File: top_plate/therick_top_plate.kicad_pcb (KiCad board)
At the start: 2 copper layers, 227.8 x 75.5 mm, 54 parts, among them U1 HOLE, U10 HOLE, U11 HOLE, U12 HOLE, U13 HOLE, U14 HOLE, U15 HOLE, U16 HOLE, U17 HOLE, U18 HOLE, U19 HOLE, U2 HOLE, U20 HOLE, U21 HOLE, U22 HOLE, U23 HOLE, U24 HOLE, U25 HOLE, U26 HOLE, U27 HOLE, U28 HOLE, U29 HOLE, U3 HOLE, U30 HOLE, U31 HOLE, U32 HOLE, U33 HOLE, U34 HOLE, U35 HOLE, U36 HOLE, U37 HOLE, U38 HOLE, U39 HOLE, U4 HOLE, U40 HOLE, U41 HOLE, U42 HOLE, U43 HOLE, U44 HOLE, U45 HOLE, U46 HOLE, U47 HOLE, U48 HOLE, U5 HOLE, U6 HOLE, U7 HOLE, U8 HOLE, U9 HOLE

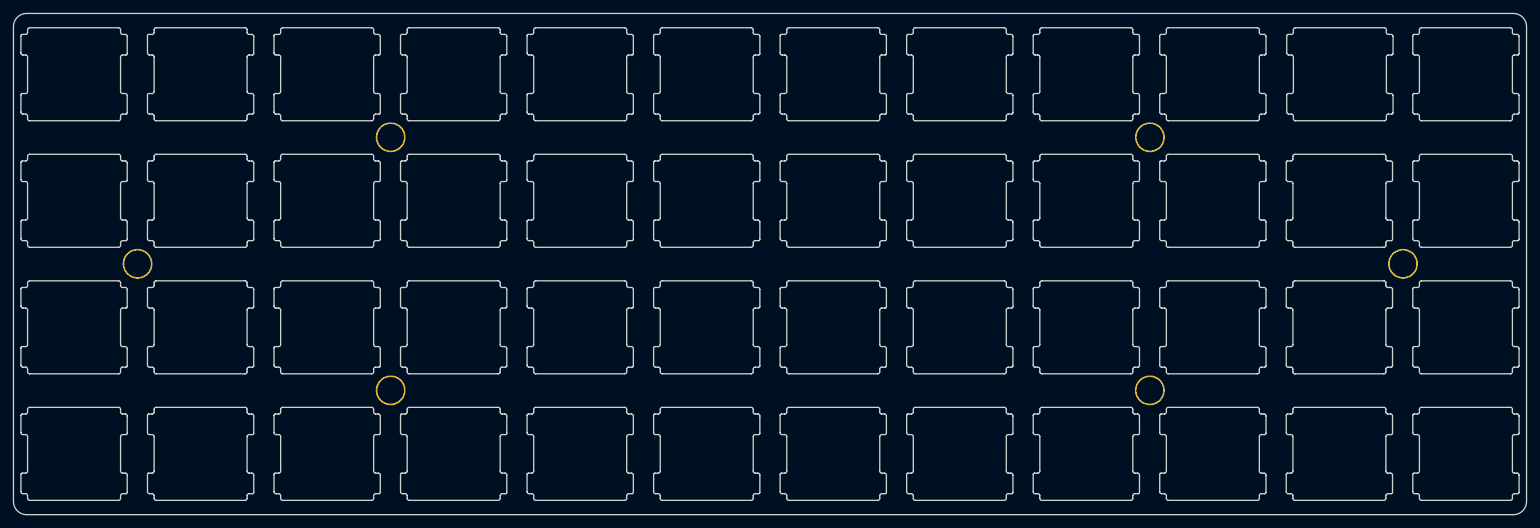
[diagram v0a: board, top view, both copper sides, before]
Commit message: Removed Type C Connector
Only uses a Pro Micro/Elite C now
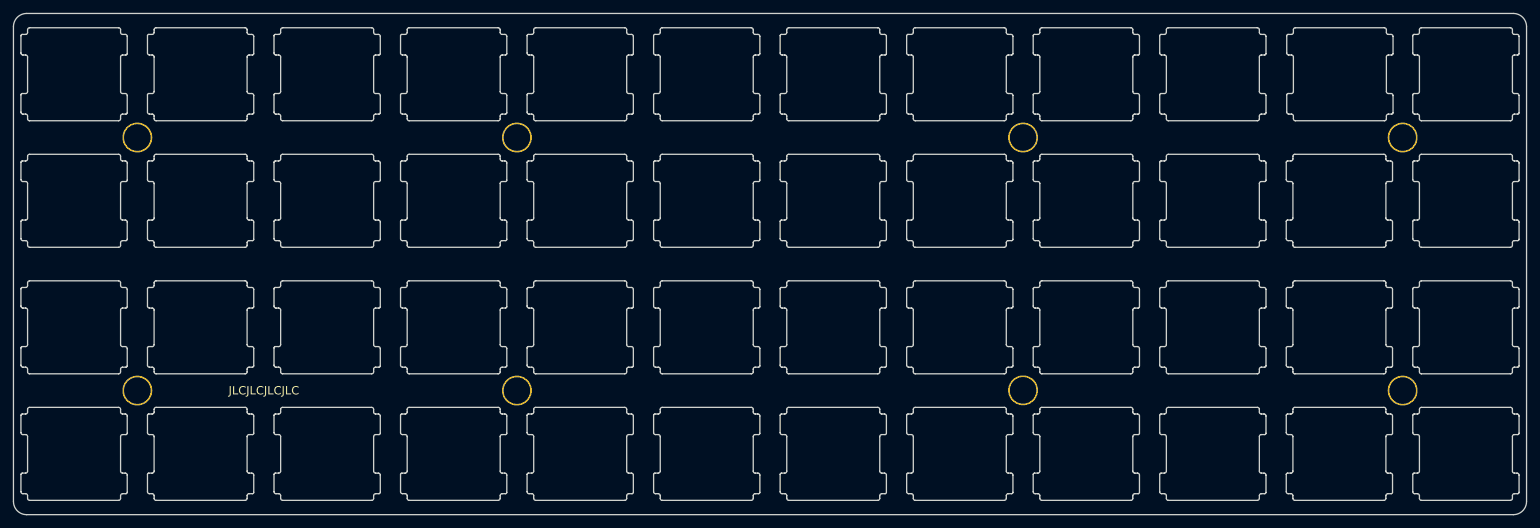
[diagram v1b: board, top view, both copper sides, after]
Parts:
- added H7: MountingHole, random-keyboard-parts:plate_hole_4mm_tht, F.Cu at (65.0, 56.0)
- added H8: MountingHole, random-keyboard-parts:plate_hole_4mm_tht, F.Cu at (255.5, 94.1)
- moved H4 19.1 mm to (198.4, 56.0)
- moved H1 19.1 mm to (65.0, 94.1)
- moved H5 19.1 mm to (198.4, 94.1)
- moved H6 19.0 mm to (255.5, 56.0)
- moved H2 19.0 mm to (122.2, 56.0)
- moved H3 19.0 mm to (122.2, 94.1)
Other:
- board text added: "JLCJLCJLCJLC"
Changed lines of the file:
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@@
   (general
     (thickness 1.6)
-    (drawings 8)
+    (drawings 9)
     (tracks 0)
     (zones 0)
-    (modules 54)
+    (modules 56)
     (nets 1)
   )
@@
     (solder_mask_min_width 0.25)
     (aux_axis_origin 0 0)
-    (visible_elements FFFFFF7F)
+    (visible_elements FFFFEF7F)
     (pcbplotparams
       (layerselection 0x010fc_ffffffff)
@@
     (uvia_drill 0.1)
   )
+  (module random-keyboard-parts:plate_hole_4mm_tht locked (layer F.Cu)
+    (at 255.5367 94.107)
+    (fp_text reference H8 (at 0.381 1.4097) (layer Dwgs.User)
+      (effects (font (size 1 1) (thickness 0.15)))
+    )
+    (fp_text value MountingHole (at 0 -0.5) (layer F.Fab)
+      (effects (font (size 1 1) (thickness 0.15)))
+    )
+    (pad 1 thru_hole circle (at 0.0508 -2.032) (size 4.5 4.5) (drill 4) (layers *.Cu *.Mask))
+  )
+  (module random-keyboard-parts:plate_hole_4mm_tht locked (layer F.Cu)
+    (at 65.0367 56.007)
+    (fp_text reference H7 (at 0.381 1.4097) (layer Dwgs.User)
+      (effects (font (size 1 1) (thickness 0.15)))
+    )
+    (fp_text value MountingHole (at 0 -0.5) (layer F.Fab)
+      (effects (font (size 1 1) (thickness 0.15)))
+    )
+    (pad 1 thru_hole circle (at 0.0508 -2.032) (size 4.5 4.5) (drill 4) (layers *.Cu *.Mask))
+  )
   (module random-keyboard-parts:MX100_slot (layer F.Cu)
     (at 55.5625 44.45)
@@
   )
   (module random-keyboard-parts:plate_hole_4mm_tht locked (layer F.Cu)
-    (at 65.0748 75.0189)
+    (at 65.0367 94.107)
     (fp_text reference H1 (at 0 1.1811) (layer Dwgs.User)
       (effects (font (size 1 1) (thickness 0.15)))
@@
   )
   (module random-keyboard-parts:plate_hole_4mm_tht locked (layer F.Cu)
-    (at 103.1748 55.9689)
+    (at 122.1867 56.007)
     (fp_text reference H2 (at 0 1.1811) (layer Dwgs.User)
       (effects (font (size 1 1) (thickness 0.15)))
@@
   )
   (module random-keyboard-parts:plate_hole_4mm_tht locked (layer F.Cu)
-    (at 103.1748 94.0689)
+    (at 122.1867 94.107)
     (fp_text reference H3 (at 0 1.1811) (layer Dwgs.User)
       (effects (font (size 1 1) (thickness 0.15)))
@@
   )
   (module random-keyboard-parts:plate_hole_4mm_tht locked (layer F.Cu)
-    (at 217.4875 55.9689)
+    (at 198.3867 56.007)
     (fp_text reference H4 (at 0 1.1811) (layer Dwgs.User)
       (effects (font (size 1 1) (thickness 0.15)))
@@
   )
   (module random-keyboard-parts:plate_hole_4mm_tht locked (layer F.Cu)
-    (at 217.4748 94.0689)
+    (at 198.3867 94.0689)
     (fp_text reference H5 (at 0 1.1811) (layer Dwgs.User)
       (effects (font (size 1 1) (thickness 0.15)))
@@
   )
   (module random-keyboard-parts:plate_hole_4mm_tht locked (layer F.Cu)
-    (at 255.5875 75.0189)
+    (at 255.5367 56.007)
     (fp_text reference H6 (at 0 1.1811) (layer Dwgs.User)
       (effects (font (size 1 1) (thickness 0.15)))
@@
     (pad 1 thru_hole circle (at 0.0508 -2.032) (size 4.5 4.5) (drill 4) (layers *.Cu *.Mask))
   )
+  (gr_text JLCJLCJLCJLC (at 84.1375 92.075) (layer F.SilkS)
+    (effects (font (size 1.25 1.25) (thickness 0.2)))
+  )
   (gr_line (start 48.41875 35.294875) (end 272.25625 35.294875) (layer Edge.Cuts) (width 0.05))
